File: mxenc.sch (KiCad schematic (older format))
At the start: 28 parts, among them J4 Conn_01x06, J6 Conn_01x06, J8 Conn_01x06 DNP, SW1 SW_Push, SW2 SW_Push, U1 IMX8MM, U10 24LC16, Y2 Crystal_GND24

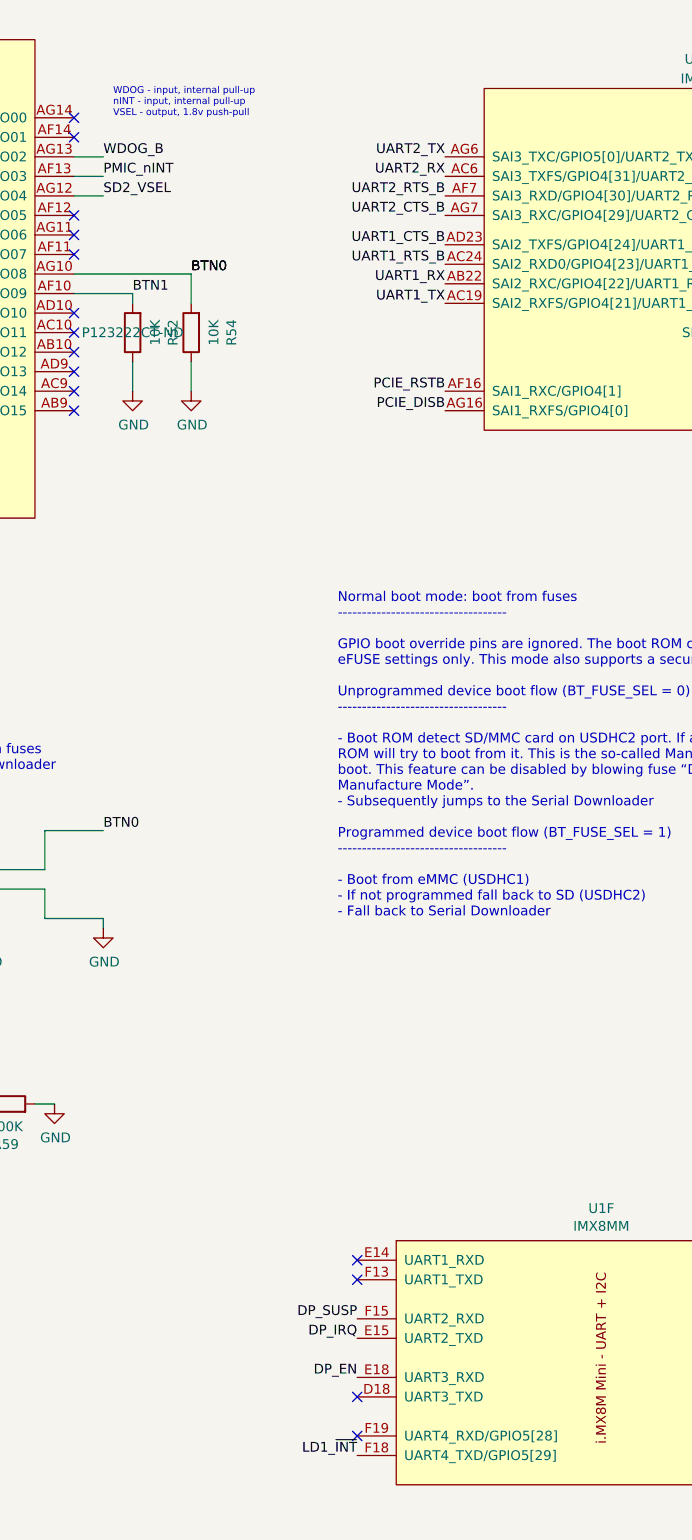
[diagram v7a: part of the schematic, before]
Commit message: rough layout, routing for emmc and csi, dsi, pcie
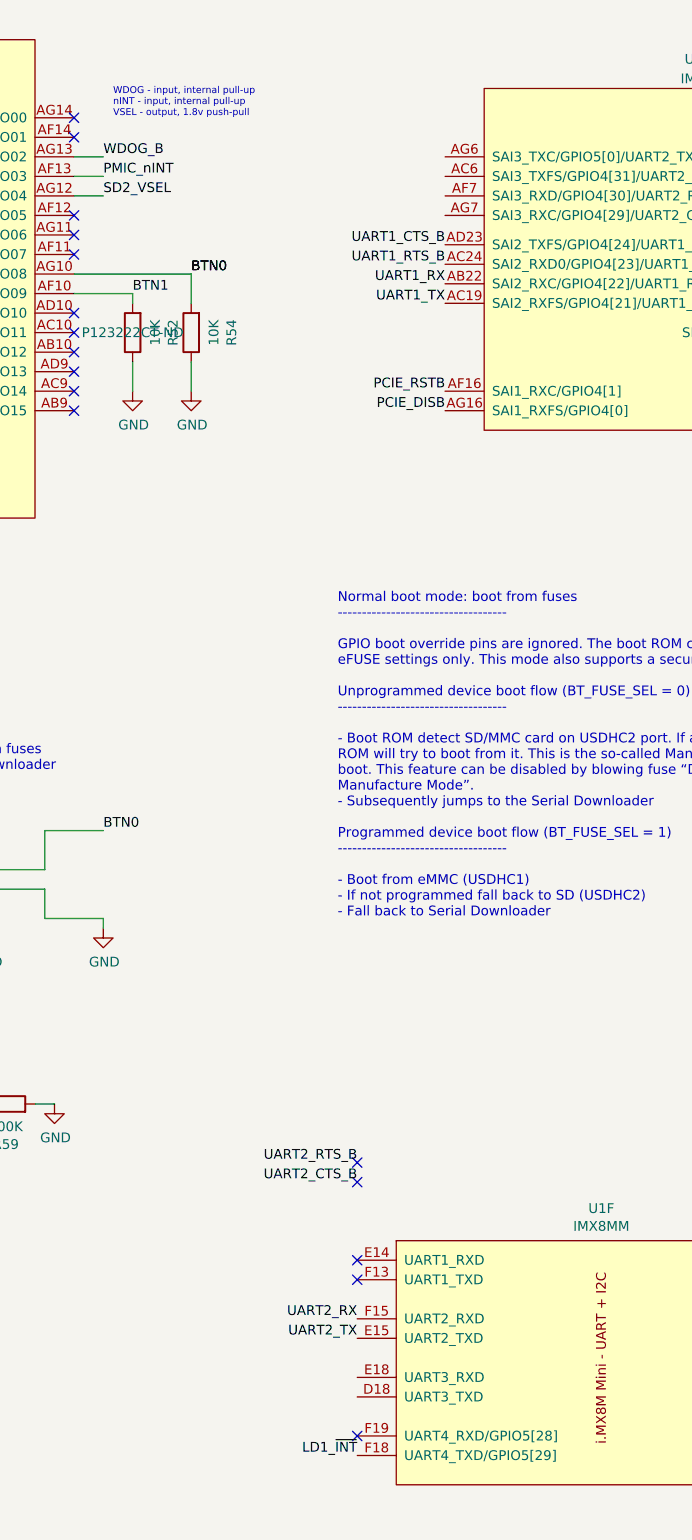
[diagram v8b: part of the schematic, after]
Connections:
- net DP_EN: no longer U1.E18 (UART3_RXD)
- net DP_IRQ: no longer U1.E15 (UART2_TXD)
- net DP_SUSP: no longer U1.F15 (UART2_RXD)
- net UART2_CTS_B: no longer U1.AG7 (SAI3_RXC/GPIO4[29]/UART2_CTS_B)
- net UART2_RTS_B: no longer U1.AF7 (SAI3_RXD/GPIO4[30]/UART2_RTS_B)
- net UART2_RX: now also U1.F15 (UART2_RXD); no longer U1.AC6 (SAI3_TXFS/GPIO4[31]/UART2_RX)
- net UART2_TX: now also U1.E15 (UART2_TXD); no longer U1.AG6 (SAI3_TXC/GPIO5[0]/UART2_TX)
- no-connect marks 35 -> 36
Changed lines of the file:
@@
 Text Label 6600 1700 2    50   ~ 0
 LED_B
-Text Label 7750 3150 2    50   ~ 0
+Text Label 7300 9200 2    50   ~ 0
 UART2_TX
-Text Label 7750 3250 2    50   ~ 0
+Text Label 7300 9100 2    50   ~ 0
 UART2_RX
-Text Label 7750 3350 2    50   ~ 0
+Text Label 7300 8300 2    50   ~ 0
 UART2_RTS_B
-Text Label 7750 3450 2    50   ~ 0
+Text Label 7300 8400 2    50   ~ 0
 UART2_CTS_B
 Text Label 7750 3900 2    50   ~ 0
@@
 	1    0    0    -1
 $EndComp
-Text Label 7300 9100 2    50   ~ 0
-DP_SUSP
 Text Label 11250 9800 0    50   ~ 0
 I2C4_SDA
@@
 Text Label 11250 8800 0    50   ~ 0
 I2C1_SCL
-Text Label 7300 9200 2    50   ~ 0
-DP_IRQ
-Text Label 7300 9400 2    50   ~ 0
-DP_EN
 NoConn ~ 7300 9700
 Text Label 7300 9800 2    50   ~ 0
 LD1_~INT
-NoConn ~ 7300 9500
 NoConn ~ 7300 8900
 NoConn ~ 7300 8800
@@
 F1 "expansion.sch" 50
 $EndSheet
+NoConn ~ 7300 8300
+NoConn ~ 7300 8400
 $EndSCHEMATC
